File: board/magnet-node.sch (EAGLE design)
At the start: 36 parts, among them IC1 HTU21D, X1 SMA-142-0701-801/806, X2 SMA-142-0711-821/826

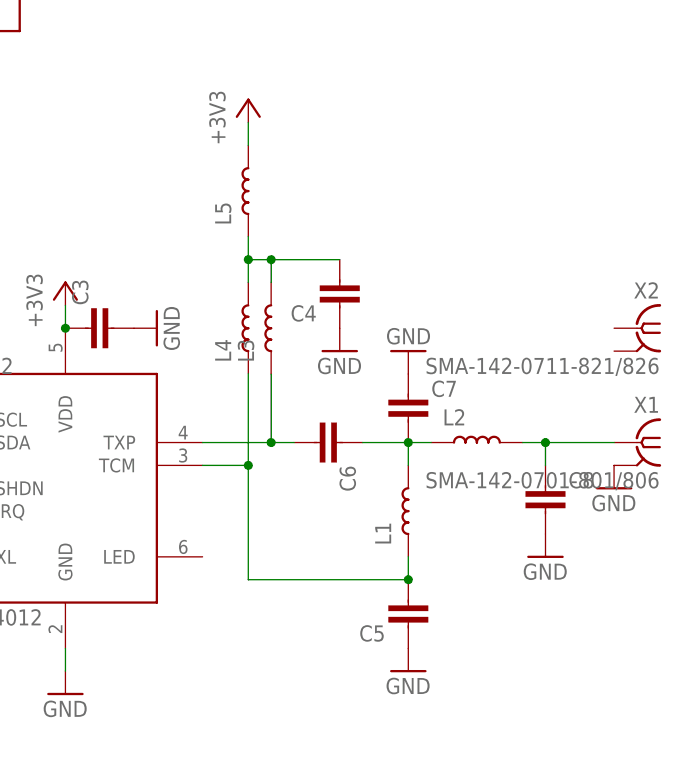
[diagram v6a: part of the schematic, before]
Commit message: adding some values and labels
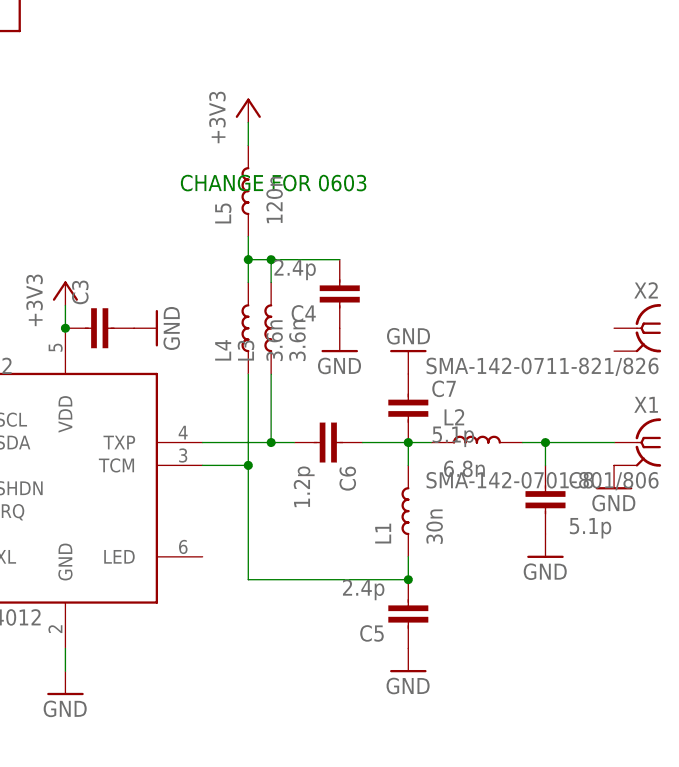
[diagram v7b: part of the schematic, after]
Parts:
- C4, C5: value (none) -> 2.4p
- C6: value (none) -> 1.2p
- C7, C8: value (none) -> 5.1p
- L1: value (none) -> 30n
- L2: value (none) -> 6.8n
- L3, L4: value (none) -> 3.6n
- L5: value (none) -> 120n
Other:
- note added: "CHANGE FOR 0603"
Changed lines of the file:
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@@
 <part name="+3V4" library="supply1" deviceset="+3V3" device=""/>
 <part name="GND8" library="supply1" deviceset="GND" device=""/>
-<part name="C4" library="passives-7351" deviceset="CAPACITOR" device="0603-N"/>
-<part name="C5" library="passives-7351" deviceset="CAPACITOR" device="0603-N"/>
-<part name="C6" library="passives-7351" deviceset="CAPACITOR" device="0603-N"/>
-<part name="C7" library="passives-7351" deviceset="CAPACITOR" device="0603-N"/>
+<part name="C4" library="passives-7351" deviceset="CAPACITOR" device="0603-N" value="2.4p"/>
+<part name="C5" library="passives-7351" deviceset="CAPACITOR" device="0603-N" value="2.4p"/>
+<part name="C6" library="passives-7351" deviceset="CAPACITOR" device="0603-N" value="1.2p"/>
+<part name="C7" library="passives-7351" deviceset="CAPACITOR" device="0603-N" value="5.1p"/>
 <part name="GND9" library="supply1" deviceset="GND" device=""/>
 <part name="+3V5" library="supply1" deviceset="+3V3" device=""/>
 <part name="GND10" library="supply1" deviceset="GND" device=""/>
 <part name="GND11" library="supply1" deviceset="GND" device=""/>
-<part name="C8" library="passives-7351" deviceset="CAPACITOR" device="0603-N"/>
+<part name="C8" library="passives-7351" deviceset="CAPACITOR" device="0603-N" value="5.1p"/>
 <part name="GND12" library="supply1" deviceset="GND" device=""/>
 <part name="X1" library="con-coax" deviceset="SMA-" device="142-0701-801/806"/>
@@
 <part name="+3V7" library="supply1" deviceset="+3V3" device=""/>
 <part name="+3V9" library="supply1" deviceset="+3V3" device=""/>
-<part name="L1" library="passives-7351" deviceset="INDUCTOR" device="0402-N"/>
-<part name="L2" library="passives-7351" deviceset="INDUCTOR" device="0402-N"/>
-<part name="L3" library="passives-7351" deviceset="INDUCTOR" device="0402-N"/>
-<part name="L4" library="passives-7351" deviceset="INDUCTOR" device="0402-N"/>
-<part name="L5" library="passives-7351" deviceset="INDUCTOR" device="0402-N"/>
+<part name="L1" library="passives-7351" deviceset="INDUCTOR" device="0402-N" value="30n"/>
+<part name="L2" library="passives-7351" deviceset="INDUCTOR" device="0402-N" value="6.8n"/>
+<part name="L3" library="passives-7351" deviceset="INDUCTOR" device="0402-N" value="3.6n"/>
+<part name="L4" library="passives-7351" deviceset="INDUCTOR" device="0402-N" value="3.6n"/>
+<part name="L5" library="passives-7351" deviceset="INDUCTOR" device="0402-N" value="120n"/>
 </parts>
 <sheets>
@@
 <text x="48.26" y="132.08" size="1.778" layer="91">remove?</text>
 <text x="109.22" y="60.96" size="1.778" layer="91" rot="R90">remove?</text>
+<text x="154.94" y="73.66" size="1.778" layer="91">CHANGE FOR 0603</text>
 </plain>
 <instances>

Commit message: small changes
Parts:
- removed SV4: (no value), Mine:MA04-1E
- added TP1, TP4: TPTP14SQ, testpad:TPTP14SQ
- L5: device passives-7351:INDUCTOR0402-N -> passives-7351:INDUCTOR0603-N
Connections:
- net N$11: now also TP1.TP
- net N$14: now also TP4.TP
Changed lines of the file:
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@@
 <part name="U$3" library="Mine" deviceset="LMT85" device=""/>
 <part name="IC1" library="Mine" deviceset="HTU21D" device=""/>
-<part name="SV4" library="Mine" deviceset="MA04-1" device="E"/>
 <part name="GND17" library="supply1" deviceset="GND" device=""/>
 <part name="C12" library="passives-7351" deviceset="CAPACITOR" device="0603-N"/>
@@
 <part name="L3" library="passives-7351" deviceset="INDUCTOR" device="0402-N" value="3.6n"/>
 <part name="L4" library="passives-7351" deviceset="INDUCTOR" device="0402-N" value="3.6n"/>
-<part name="L5" library="passives-7351" deviceset="INDUCTOR" device="0402-N" value="120n"/>
+<part name="L5" library="passives-7351" deviceset="INDUCTOR" device="0603-N" value="120n"/>
+<part name="TP4" library="testpad" deviceset="TP" device="TP14SQ"/>
+<part name="TP1" library="testpad" deviceset="TP" device="TP14SQ"/>
 </parts>
 <sheets>
@@
 <instance part="U$3" gate="G$1" x="134.62" y="99.06"/>
 <instance part="IC1" gate="G$1" x="48.26" y="104.14"/>
-<instance part="SV4" gate="1" x="-17.78" y="30.48"/>
 <instance part="GND17" gate="1" x="53.34" y="88.9"/>
 <instance part="C12" gate="G$1" x="58.42" y="119.38" rot="R90"/>
@@
 <instance part="L4" gate="G$1" x="162.56" y="58.42" rot="R90"/>
 <instance part="L5" gate="G$1" x="162.56" y="73.66" rot="R90"/>
+<instance part="TP4" gate="G$1" x="68.58" y="45.72" rot="R270"/>
+<instance part="TP1" gate="G$1" x="68.58" y="48.26" rot="R270"/>
 </instances>
 <busses>
@@
 <pinref part="U$1" gate="G$1" pin="P1.1"/>
 <wire x1="63.5" y1="48.26" x2="66.04" y2="48.26" width="0.1524" layer="91"/>
+<pinref part="TP1" gate="G$1" pin="TP"/>
 </segment>
 </net>
@@
 <pinref part="U$1" gate="G$1" pin="P1.2"/>
 <wire x1="66.04" y1="45.72" x2="63.5" y2="45.72" width="0.1524" layer="91"/>
-</segment>
-</net>
+<pinref part="TP4" gate="G$1" pin="TP"/>
+</segment>
+</net>
